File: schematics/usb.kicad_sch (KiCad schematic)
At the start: 7 parts, among them J1 USB_C_Receptacle_USB2.0_16P, U3 USBLC6-2SC6

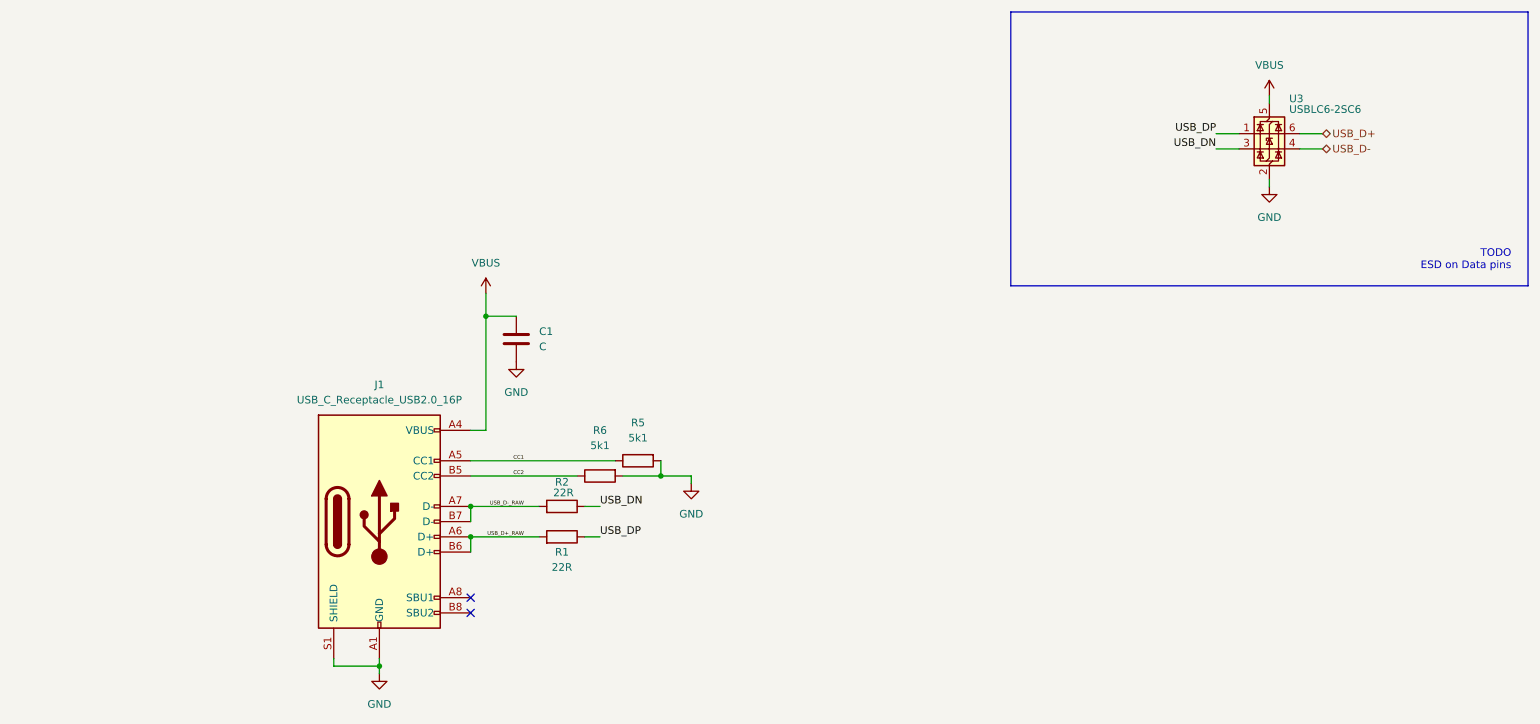
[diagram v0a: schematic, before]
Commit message: Add LED driver ic TLC59208F
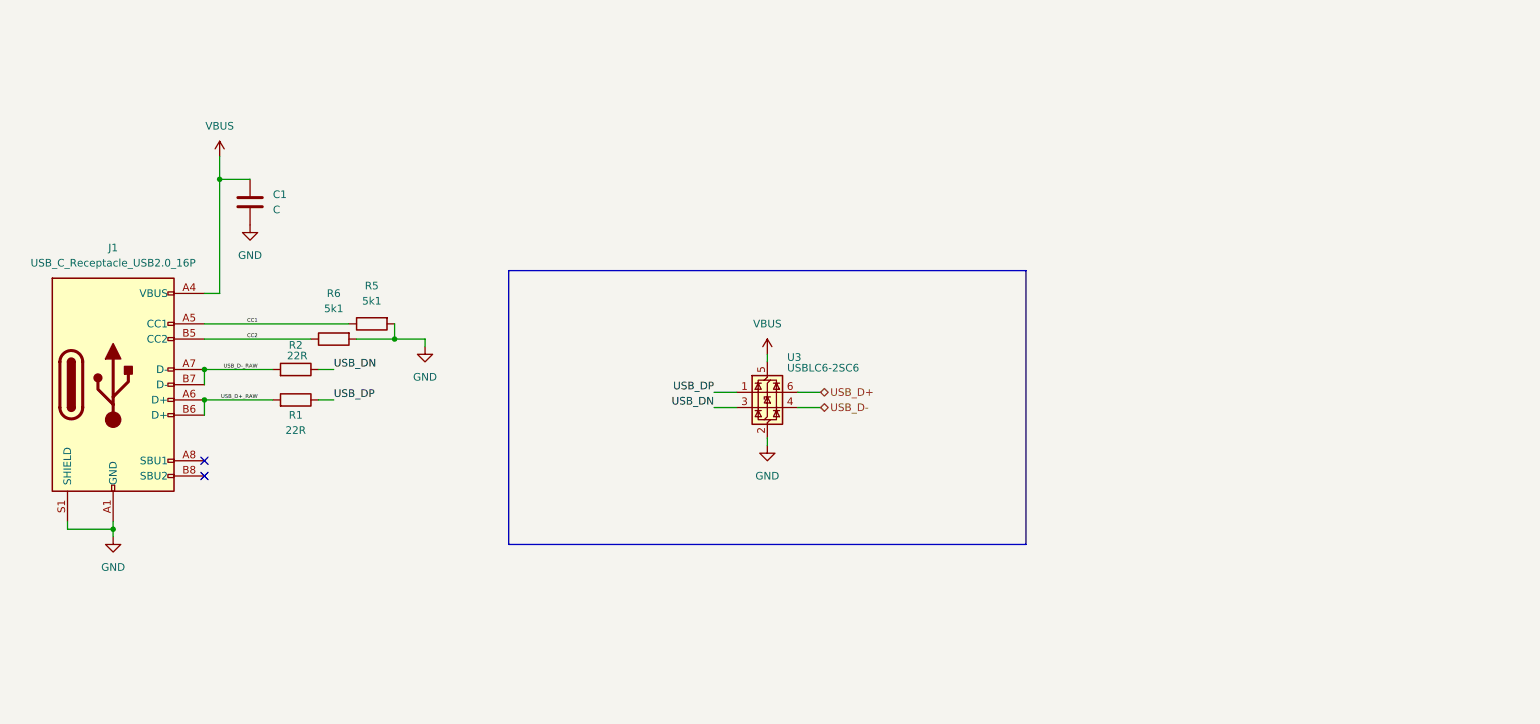
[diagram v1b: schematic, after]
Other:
- note removed: "TODO ESD on Data pins"
- moved on the sheet: C1, J1, R1, R2, R5, R6, U3

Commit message: Fix layout, rewiring, and clearances
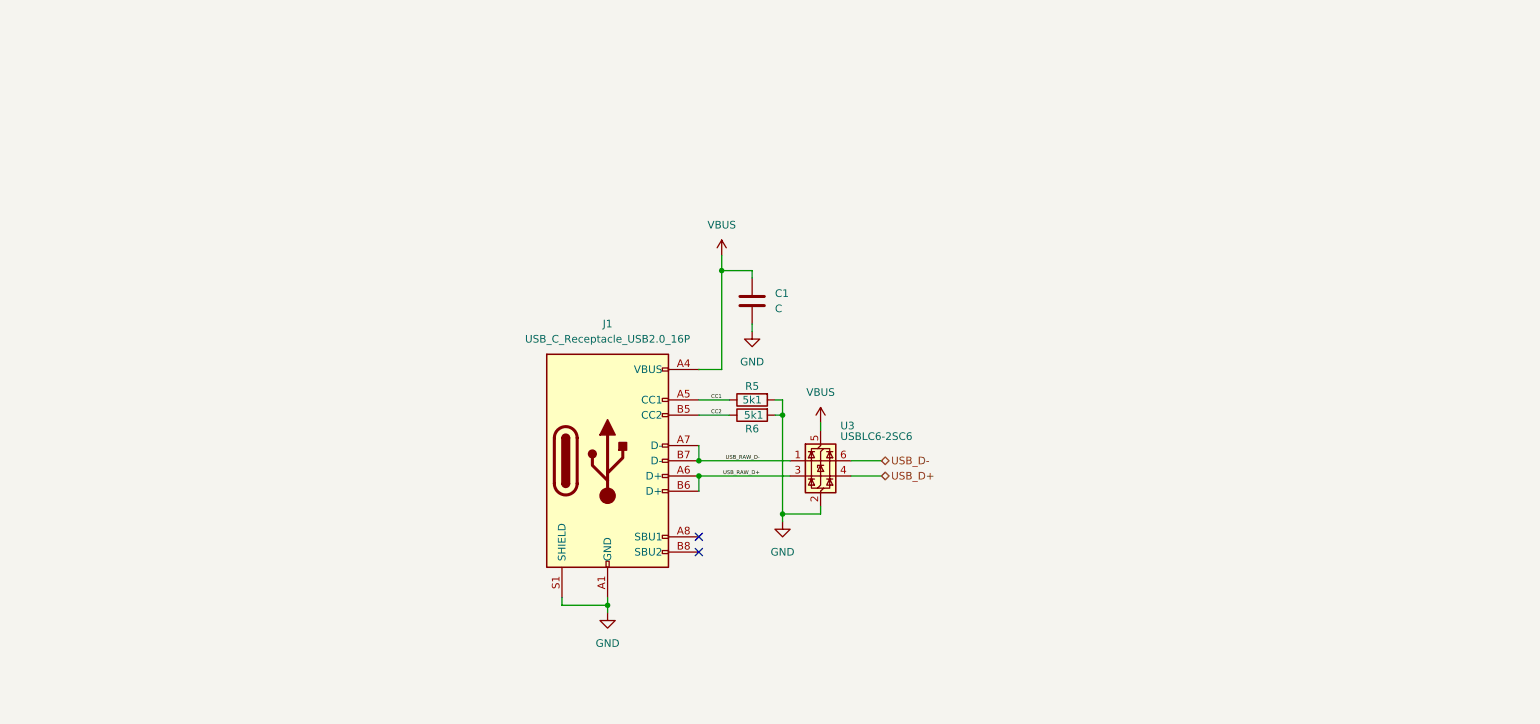
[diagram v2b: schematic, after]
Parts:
- removed R1, R2: 22R, Resistor_SMD:R_0603_1608Metric, symbol Device:R
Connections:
- net USB_DN is gone; now on net USB_RAW_D+: U3.3 (I/O2)
- net USB_DP is gone; now on net USB_RAW_D-: U3.1 (I/O1)
- net USB_D+: now also U3.4 (I/O2); no longer U3.6 (I/O1)
- net USB_D-: now also U3.6 (I/O1); no longer U3.4 (I/O2)
- net USB_D+_RAW renamed USB_RAW_D+
- net USB_D-_RAW renamed USB_RAW_D-
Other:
- moved on the sheet: C1, J1, R5, R6, U3

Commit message: temp
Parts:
- J1: value USB_C_Receptacle_USB2.0_16P -> TYPE-C 16PIN 2MD(073); LCSC (none) -> C2765186
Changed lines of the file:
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@@
 			)
 		)
-		(property "Value" "USB_C_Receptacle_USB2.0_16P"
+		(property "Value" "TYPE-C 16PIN 2MD(073)"
 			(at 128.27 69.85 0)
 			(effects
@@
 			(at 128.27 90.17 0)
 			(effects
+				(font
+					(size 1.27 1.27)
+				)
+				(hide yes)
+			)
+		)
+		(property "LCSC" "C2765186"
+			(at 128.27 90.17 0)
+			(effects
